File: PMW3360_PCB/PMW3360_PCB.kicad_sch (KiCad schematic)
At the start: 20 parts, among them J1 Conn_01x08, U1 PMW3360DM-T2QU, U2 TPS73601DBV

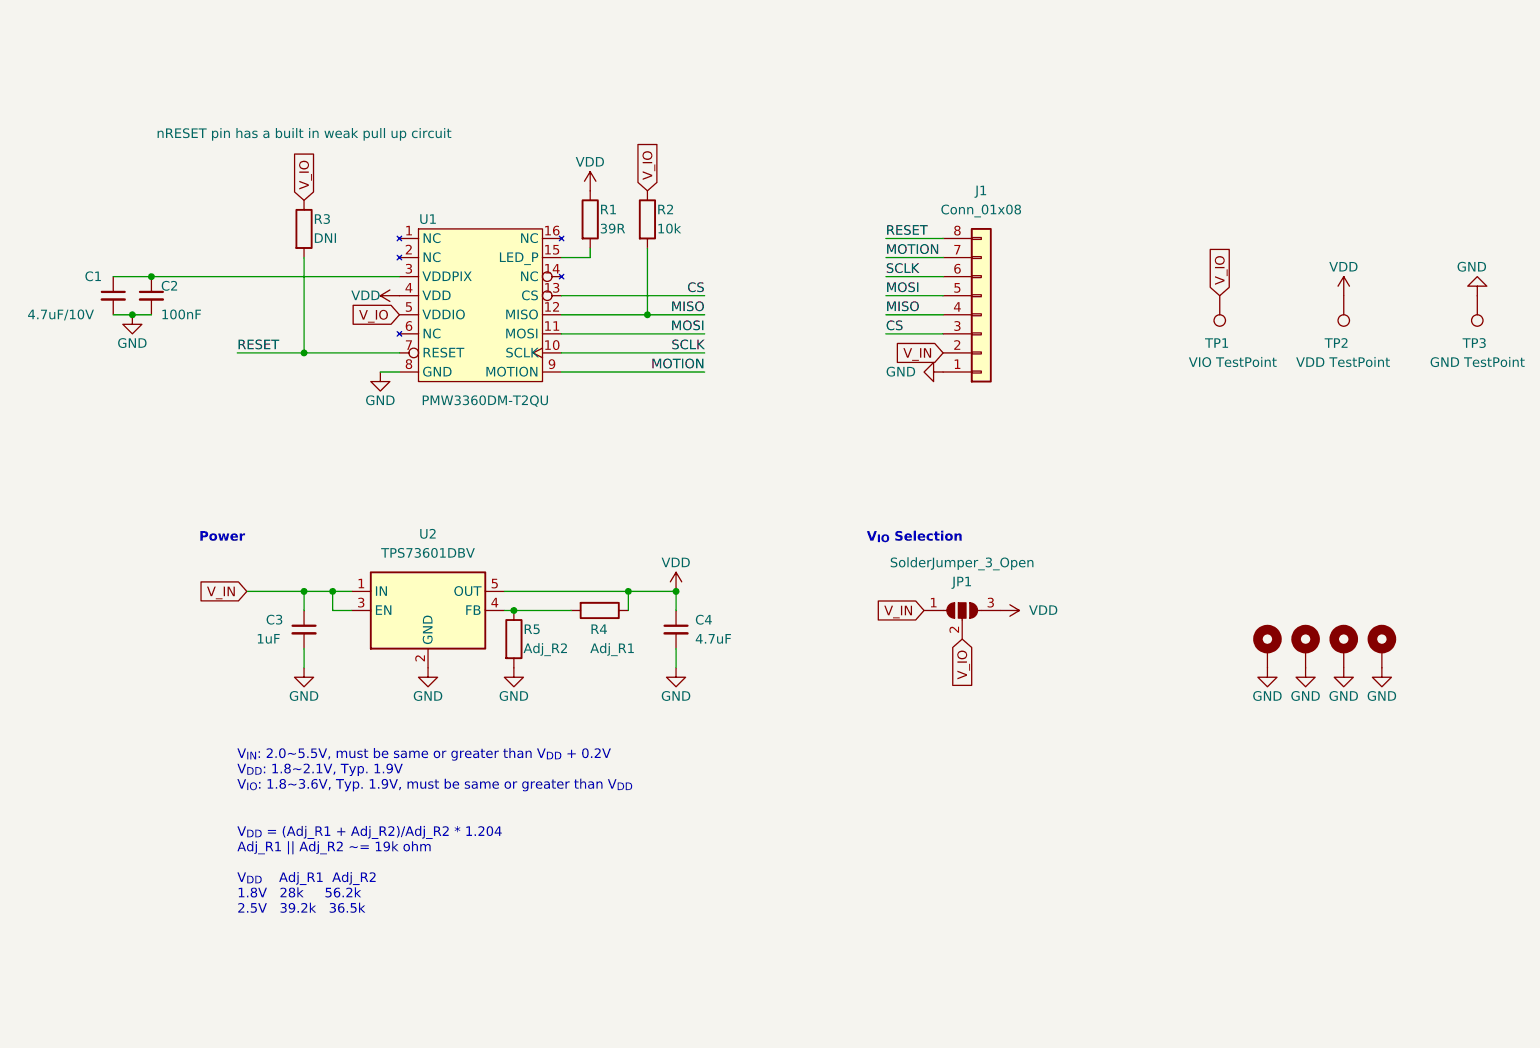
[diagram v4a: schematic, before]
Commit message: Reduce board size
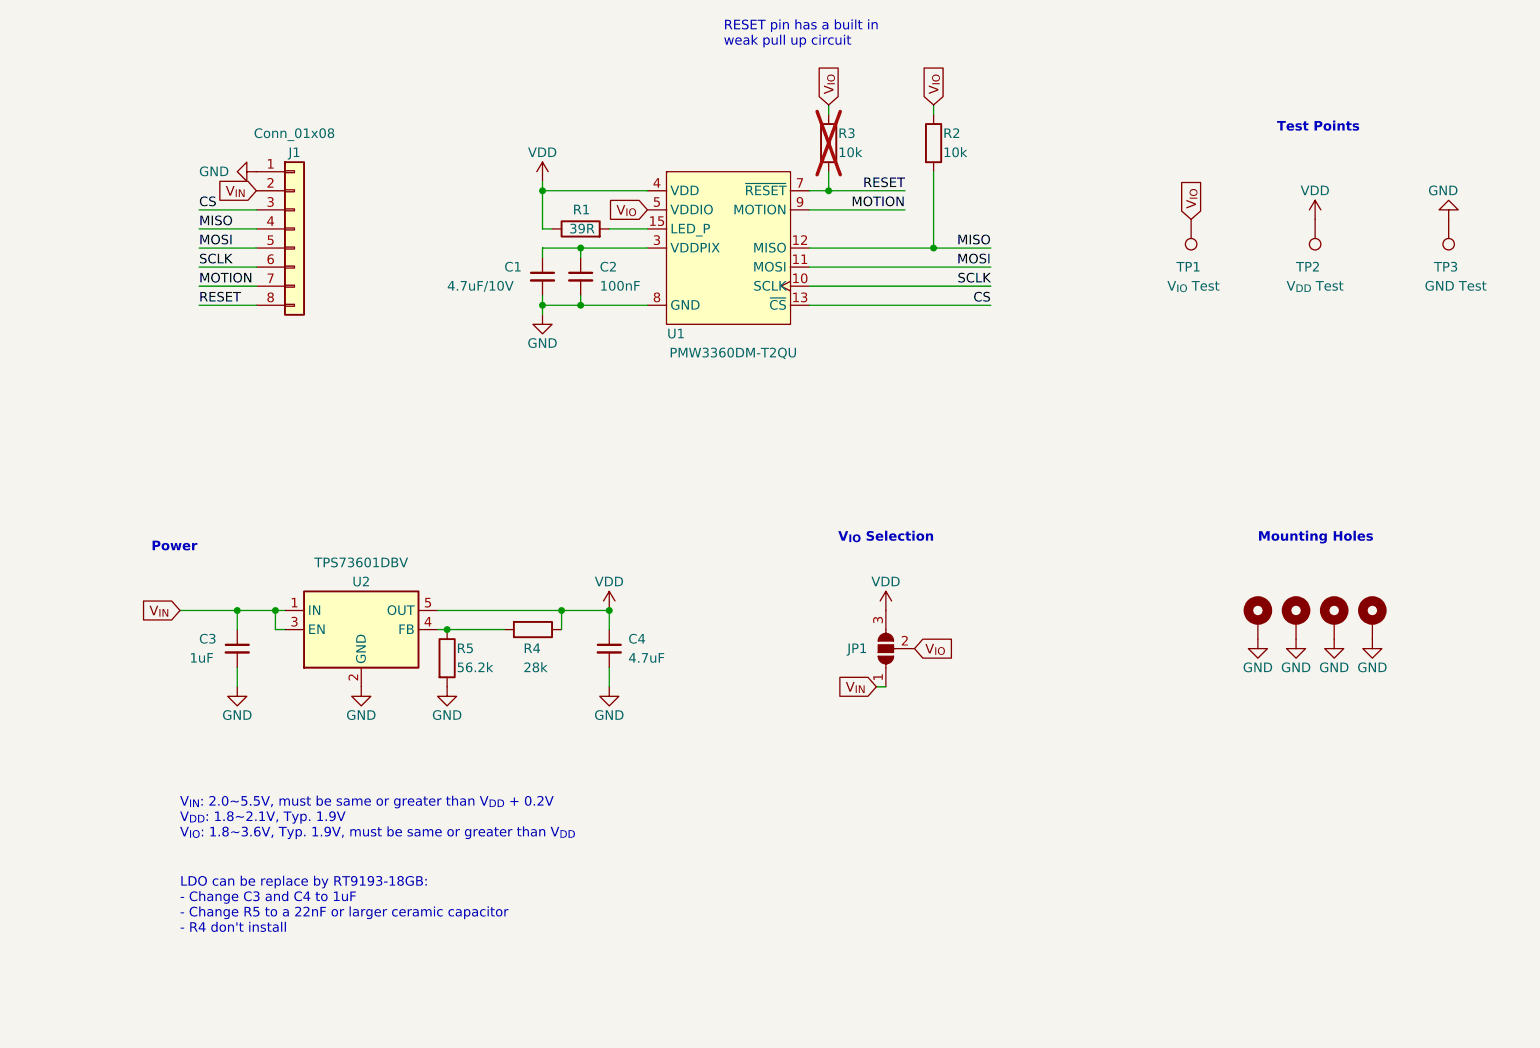
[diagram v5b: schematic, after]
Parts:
- J1: footprint ErgoSNM_Keyboard:FPC_8P_0.5mm_AFC01-S08FCA-00 -> PMW3360_PCB:FPC_8P_0.5mm_AFC01-S08FCA-00
- JP1: footprint Jumper:SolderJumper-3_P1.3mm_Open_Pad1.0x1.5mm_NumberLabels -> Jumper:SolderJumper-3_P1.3mm_Open_RoundedPad1.0x1.5mm_NumberLabels
- R3: value DNI -> 10k; Note nRESET pin has a built in weak pull up circuit -> (none); now not fitted
- R4: value Adj_R1 -> 28k
- R5: value Adj_R2 -> 56.2k
- TP1: value VIO TestPoint -> V_{IO} Test; footprint TestPoint:TestPoint_Pad_D1.5mm -> TestPoint:TestPoint_Pad_D1.0mm
- TP2: value VDD TestPoint -> V_{DD} Test; footprint TestPoint:TestPoint_Pad_D1.5mm -> TestPoint:TestPoint_Pad_D1.0mm
- TP3: value GND TestPoint -> GND Test; footprint TestPoint:TestPoint_Pad_D1.5mm -> TestPoint:TestPoint_Pad_D1.0mm
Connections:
- net V_IN renamed V_{IN}
- net V_IO renamed V_{IO}
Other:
- note added: "LDO can be replace by RT9193-18GB: - Change C3 and C4 to 1uF - Change R5 to a 22nF or larger ceramic capacitor - R4 don't install"
- note added: "Mounting Holes"
- note added: "RESET pin has a built in weak pull up circuit"
- note added: "Test Points"
- note removed: "V_{DD} = (Adj_R1 + Adj_R2)/Adj_R2 * 1.204 Adj_R1 || Adj_R2 ~= 19k ohm V_{DD} Adj_R1 Adj_R2 1.8V 28k 56.2k 2.5V 39.2k 36.5k"
- moved on the sheet: C1, C2, C3, C4, J1, JP1, R1, R2, R4, R5, TP1, TP2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

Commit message: Update schematic
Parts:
- J1: value Conn_01x08 -> Interface
- TP1: value V_{IO} Test -> V_{IO}
- TP2: value V_{DD} Test -> V_{DD}
- TP3: value GND Test -> GND
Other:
- note added: "LDO can be replace by RT9193-18GB: - Change C3 and C4 to 1uF. - Change R5 to a 22nF or larger ceramic capacitor. - R4 don't install."
- note added: "Operating Voltage Range VIN: 2.0~5.5V, must be same or greater than V_{DD} + 0.2V VDD: 1.8~2.1V, Typ. 1.9V VIO: 1.8~3.6V, Typ. 1.9V, must be same or greater than V_{DD}"
- note added: "Reserved, ~{RESET} pin has a built in weak pull up circuit."
- note removed: "LDO can be replace by RT9193-18GB: - Change C3 and C4 to 1uF - Change R5 to a 22nF or larger ceramic capacitor - R4 don't install"
- note removed: "RESET pin has a built in weak pull up circuit"
- note removed: "V_{IN}: 2.0~5.5V, must be same or greater than V_{DD} + 0.2V V_{DD}: 1.8~2.1V, Typ. 1.9V V_{IO}: 1.8~3.6V, Typ. 1.9V, must be same or greater than V_{DD}"
- company: (none) -> SideraKB
- moved on the sheet: C1, C2, C3, C4, J1, JP1, R1, R2, R3, R4, R5, TP1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
